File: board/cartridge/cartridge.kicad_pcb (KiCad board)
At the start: 4 copper layers, 58.4 x 56 mm, 57 parts, among them J1 TF-115-BCP9, J2 HC-TYPE-C-16P-01B, P1 Card Edge, Q1 DMG2301L, SW1 K3-1410S, SW2 K3-1410S, U1 AMS1117-3.3, U10 TPS2041B, U11 LM66100DCK, U12 LM66100DCK, U2 ESP32-S3-WROOM-1U, U3 TUSB321, U4 TXS0108E, U5 74LVC245, U6 74LVC1G17, U7 74LVC245, U8 74LVC245, U9 PCM5100

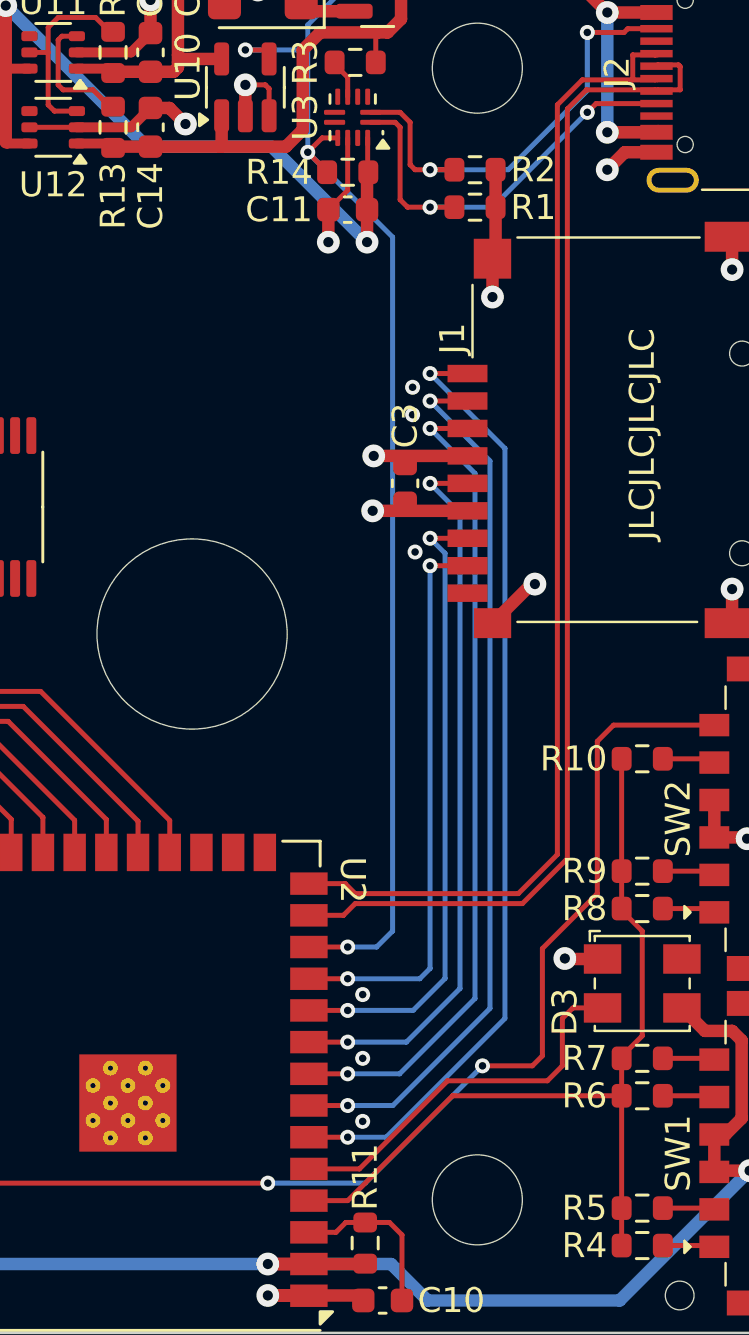
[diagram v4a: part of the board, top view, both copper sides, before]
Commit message: Add 32 kHz crystal.
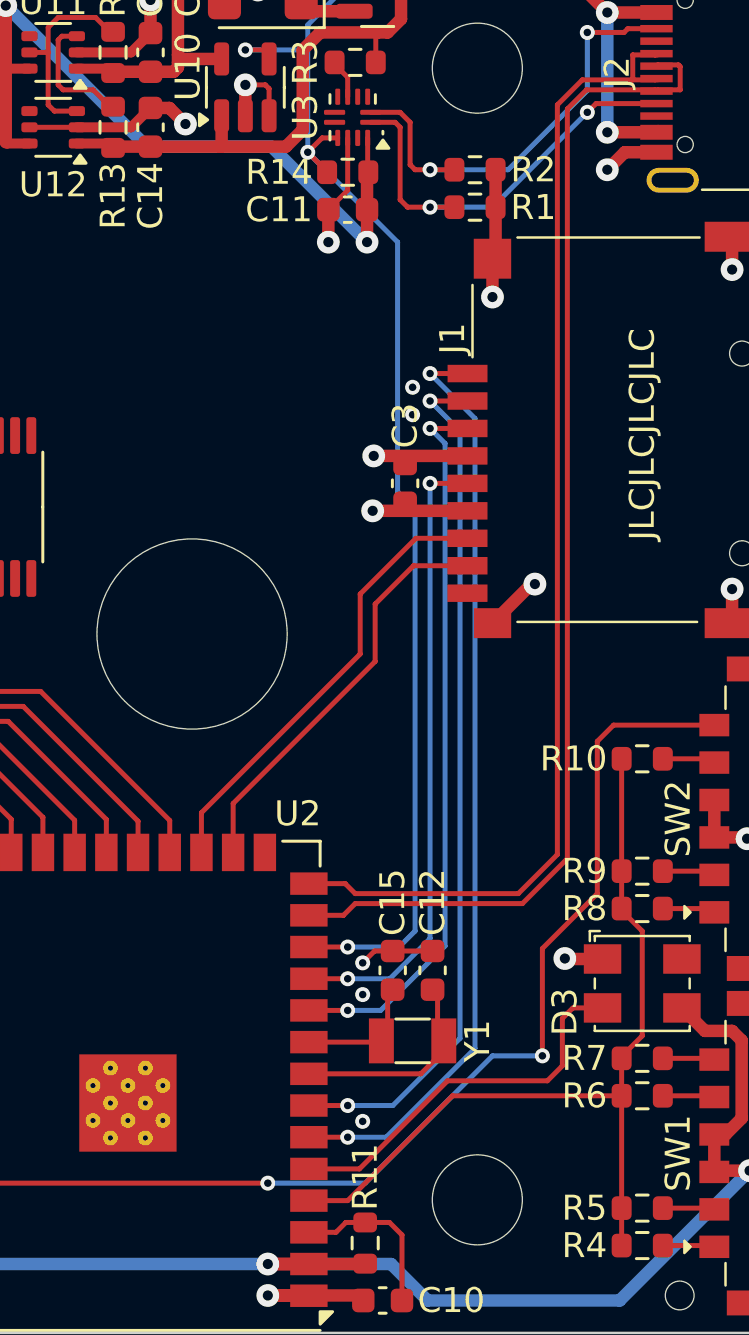
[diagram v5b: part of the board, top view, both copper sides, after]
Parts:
- added C12: 15p, Capacitor_SMD:C_0603_1608Metric, F.Cu at (163.6, 113.5)
- added C15: 15p, Capacitor_SMD:C_0603_1608Metric, F.Cu at (162.0, 113.5)
- added Y1: FC-135 32.768KHz 12.5pF, Crystal:Crystal_SMD_3215-2Pin_3.2x1.5mm, F.Cu at (162.8, 116.3)
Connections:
- U2 pad 10: /SD_DAT0 -> /SD_CMD
- U2 pad 11: /SD_DAT1 -> /SD_CLK
- U2 pad 16: unconnected-(U2-GPIO46-Pad16) -> /SD_DAT1
- U2 pad 17: unconnected-(U2-GPIO9-Pad17) -> /SD_DAT0
- U2 pad 8: /SD_CMD -> /XTAL_32K_P
- U2 pad 9: /SD_CLK -> /XTAL_32K_N
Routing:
- net /XTAL_32K_P: track 0.00 -> 7.76 mm
- net /SD_DAT0: track 25.4 -> 18.2 mm, vias 2 -> 0
- net /SD_DAT1: track 22.7 -> 16.6 mm, vias 2 -> 0
- net /XTAL_32K_N: track 0.00 -> 4.58 mm
- net /SD_CMD: track 33.0 -> 29.0 mm
- net /SD_CLK: track 29.2 -> 25.3 mm
- net GND: track 93.1 -> 96.1 mm, vias 58 -> 57
- net /USB_ID: track 51.1 -> 52.3 mm
- net /SD_DAT3: track 35.7 -> 34.7 mm
- net /SD_DAT2: track 38.4 -> 37.4 mm

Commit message: Start working on Li-Poly battery.
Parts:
- added C17: 1u, Capacitor_SMD:C_0603_1608Metric, F.Cu at (145.3, 76.7)
- added C18: 1u, Capacitor_SMD:C_0603_1608Metric, F.Cu at (131.0, 65.5)
- added C19: 1u, Capacitor_SMD:C_0603_1608Metric, F.Cu at (145.3, 79.7)
- added C20: 1u, Capacitor_SMD:C_0603_1608Metric, F.Cu at (135.9, 79.1)
- added J3: SM02B-SRSS, Connector_JST:JST_SH_SM02B-SRSS-TB_1x02-1MP_P1.00mm_Horizontal, F.Cu at (136.0, 75.0)
- added R15: 10k, Resistor_SMD:R_0603_1608Metric, F.Cu at (143.8, 76.7)
- added R16: 10k, Resistor_SMD:R_0603_1608Metric, F.Cu at (143.8, 79.7)
- added R17: 5k6, Resistor_SMD:R_0603_1608Metric, F.Cu at (144.3, 65.6)
- added R18: 10k, Resistor_SMD:R_0603_1608Metric, F.Cu at (144.3, 68.1)
- added U13: LM66100DCK, Package_TO_SOT_SMD:SOT-363_SC-70-6, F.Cu at (141.4, 76.7)
- added U14: LM66100DCK, Package_TO_SOT_SMD:SOT-363_SC-70-6, F.Cu at (141.4, 79.7)
- added U15: BQ21040DBV, Package_TO_SOT_SMD:SOT-23-6, F.Cu at (136.5, 81.9)
- moved C1 31.2 mm to (170.7, 58.8)
- moved C2 31.2 mm to (162.8, 64.8)
- moved U1 31.2 mm to (164.8, 60.0)
- renumbered D3 to D1, R4 to R1, R1 to R10, R2 to R11, R5 to R2, R6 to R3, R7 to R4, R8 to R5, R9 to R6, R10 to R7, R3 to R8, R11 to R9
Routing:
- net Net-(U13-VOUT): track 0.00 -> 11.2 mm, vias 0 -> 1
- net GND: track 96.1 -> 105.3 mm, vias 57 -> 59
- net +3V3: track 152.8 -> 144.0 mm, vias 4 -> 5
- net Net-(U13-ST): track 0.00 -> 8.11 mm
- net +BATT: track 0.00 -> 7.03 mm
- net Net-(U13-~{CE}): track 0.00 -> 5.17 mm
- net +5V: track 34.5 -> 33.2 mm
- net +5V_HOST: track 78.7 -> 77.7 mm
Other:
- board text added: "+ - Battery Li-Poly JST SH"
- board text added: "- +"

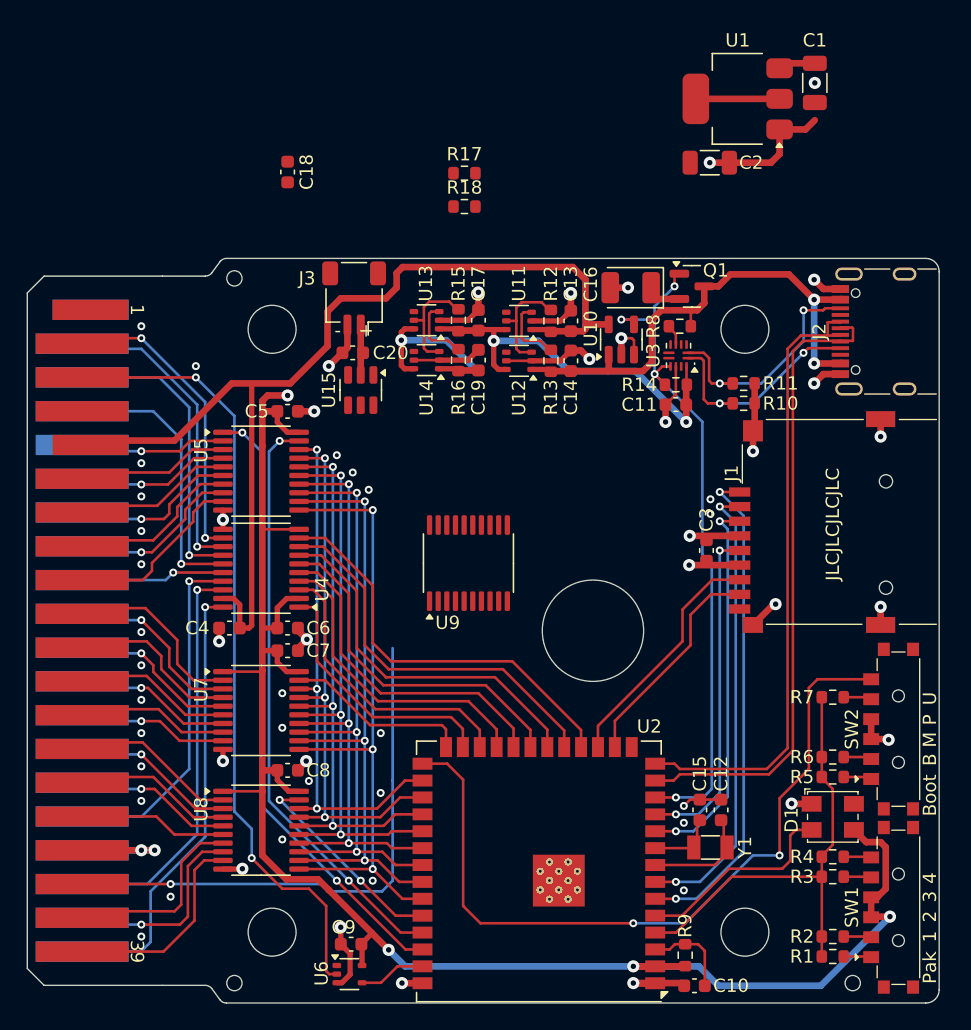
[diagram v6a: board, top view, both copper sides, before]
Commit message: Roll back adding Li-Poly battery.
This reverts commit 081752ba55a88da4e16a76dc68d1f4d967b2094e.
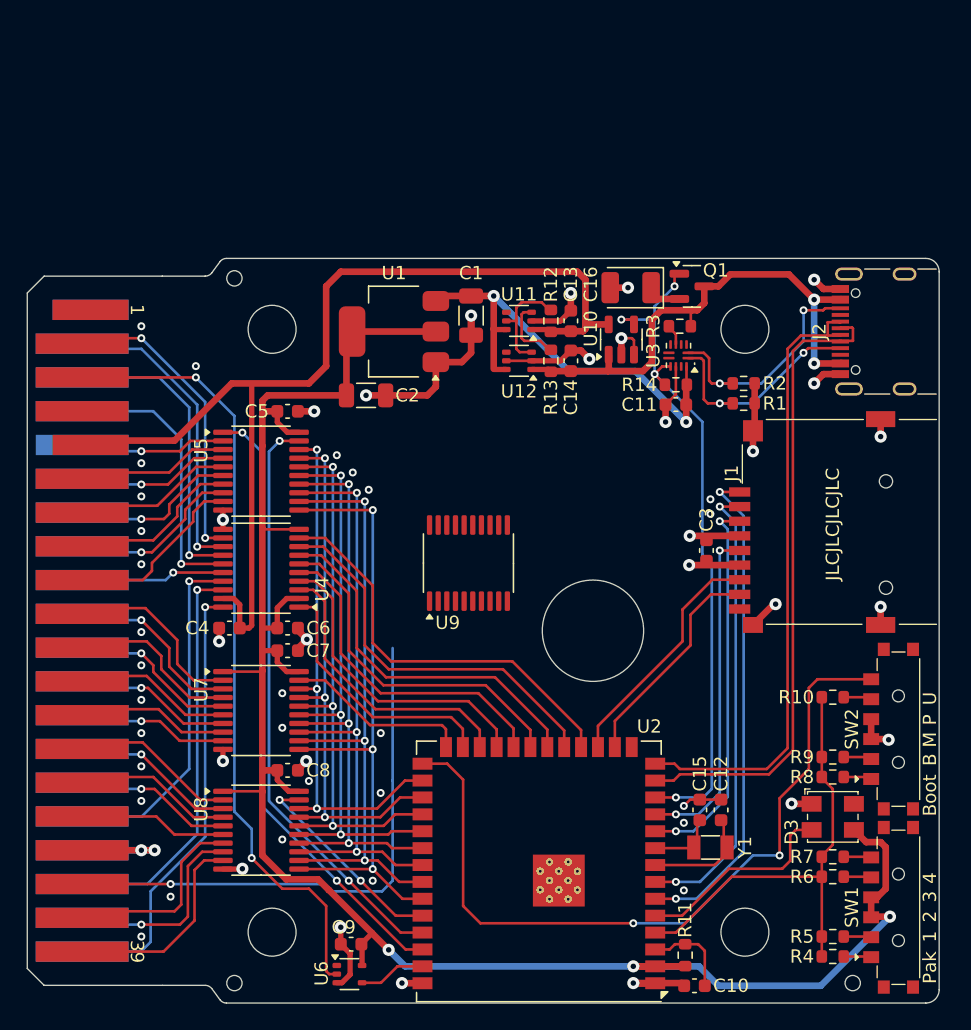
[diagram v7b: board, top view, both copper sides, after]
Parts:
- removed C17, C18, C19, C20: 1u, Capacitor_SMD:C_0603_1608Metric
- removed J3: SM02B-SRSS, Connector_JST:JST_SH_SM02B-SRSS-TB_1x02-1MP_P1.00mm_Horizontal
- removed R15, R16, R18: 10k, Resistor_SMD:R_0603_1608Metric
- removed R17: 5k6, Resistor_SMD:R_0603_1608Metric
- removed U13, U14: LM66100DCK, Package_TO_SOT_SMD:SOT-363_SC-70-6
- removed U15: BQ21040DBV, Package_TO_SOT_SMD:SOT-23-6
- moved C1 31.2 mm to (144.8, 76.3)
- moved C2 31.2 mm to (136.9, 82.3)
- moved U1 31.2 mm to (139.0, 77.5)
- renumbered D1 to D3, R10 to R1, R7 to R10, R9 to R11, R11 to R2, R8 to R3, R1 to R4, R2 to R5, R3 to R6, R4 to R7, R5 to R8, R6 to R9
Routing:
- net Net-(U13-VOUT): track 11.2 -> 0.00 mm, vias 1 -> 0
- net GND: track 105.3 -> 96.1 mm, vias 59 -> 57
- net +3V3: track 144.0 -> 152.8 mm, vias 5 -> 4
- net Net-(U13-ST): track 8.11 -> 0.00 mm
- net +BATT: track 7.03 -> 0.00 mm
- net Net-(U13-~{CE}): track 5.17 -> 0.00 mm
- net +5V: track 33.2 -> 34.5 mm
- net +5V_HOST: track 77.7 -> 78.7 mm
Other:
- board text removed: "+ - Battery Li-Poly JST SH"
- board text removed: "- +"

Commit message: Remove watch crystal and audio DAC.
These can be implemented later; they're not needed
for a first-gen prototype to determine whether the
ESP32-S3 will even be able to bit-bang the bus.
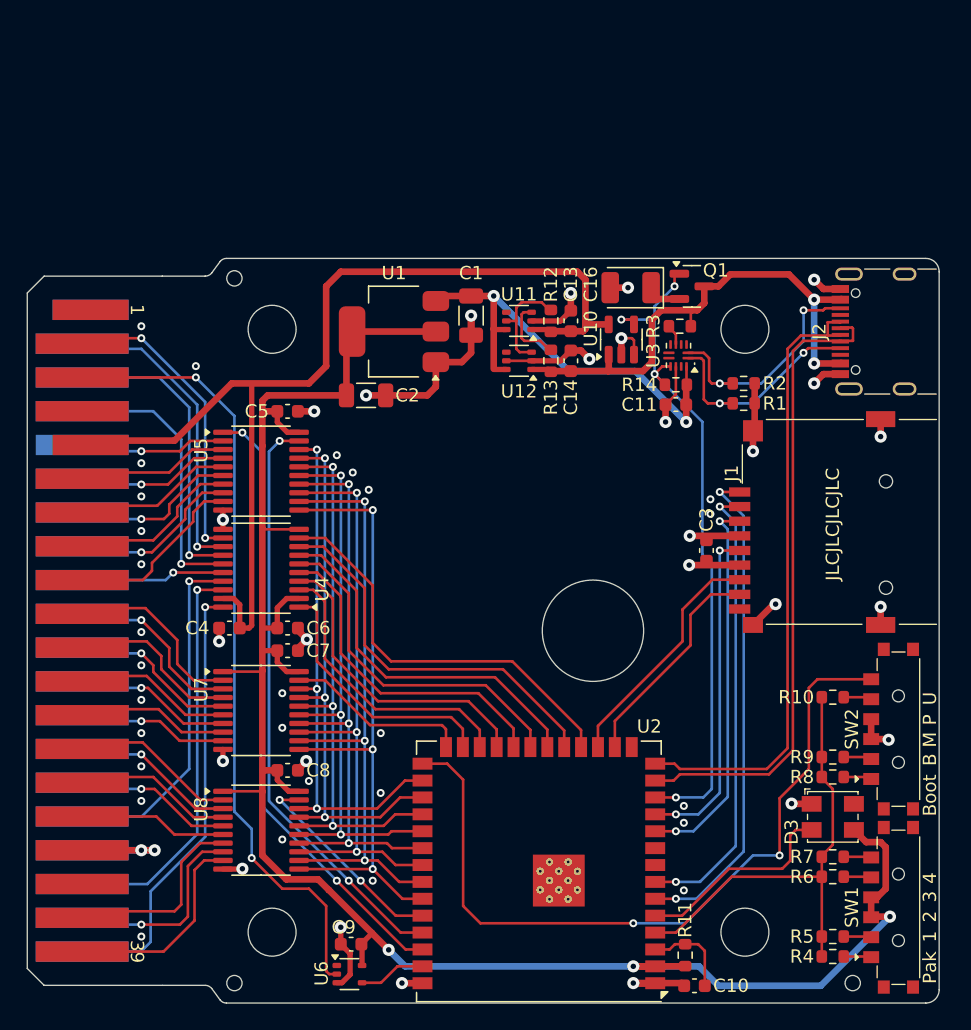
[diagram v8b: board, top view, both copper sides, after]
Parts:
- removed C12, C15: 15p, Capacitor_SMD:C_0603_1608Metric
- removed U9: PCM5100, Package_SO:TSSOP-20_4.4x6.5mm_P0.65mm
- removed Y1: FC-135 32.768KHz 12.5pF, Crystal:Crystal_SMD_3215-2Pin_3.2x1.5mm
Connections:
- U2 pad 8: /XTAL_32K_P -> unconnected-(U2-XTAL_32K_P-Pad8)
- U2 pad 9: /XTAL_32K_N -> unconnected-(U2-XTAL_32K_N-Pad9)
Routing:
- net /Host/SND: track 41.5 -> 0.00 mm, vias 1 -> 0
- net /XTAL_32K_P: track 7.76 -> 0.00 mm
- net /XTAL_32K_N: track 4.58 -> 0.00 mm
- net GND: track 96.1 -> 93.1 mm, vias 57 -> 56
